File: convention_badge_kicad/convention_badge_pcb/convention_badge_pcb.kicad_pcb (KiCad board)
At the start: 2 copper layers, 11 parts, among them J1 E_Paper_Display, J2 3.7V Battery, SW1 SW_Push, SW2 SW_Push, SW3 SW_Push, SW4 SW_SPST, U1 XIAO-ESP32-C3-DIP

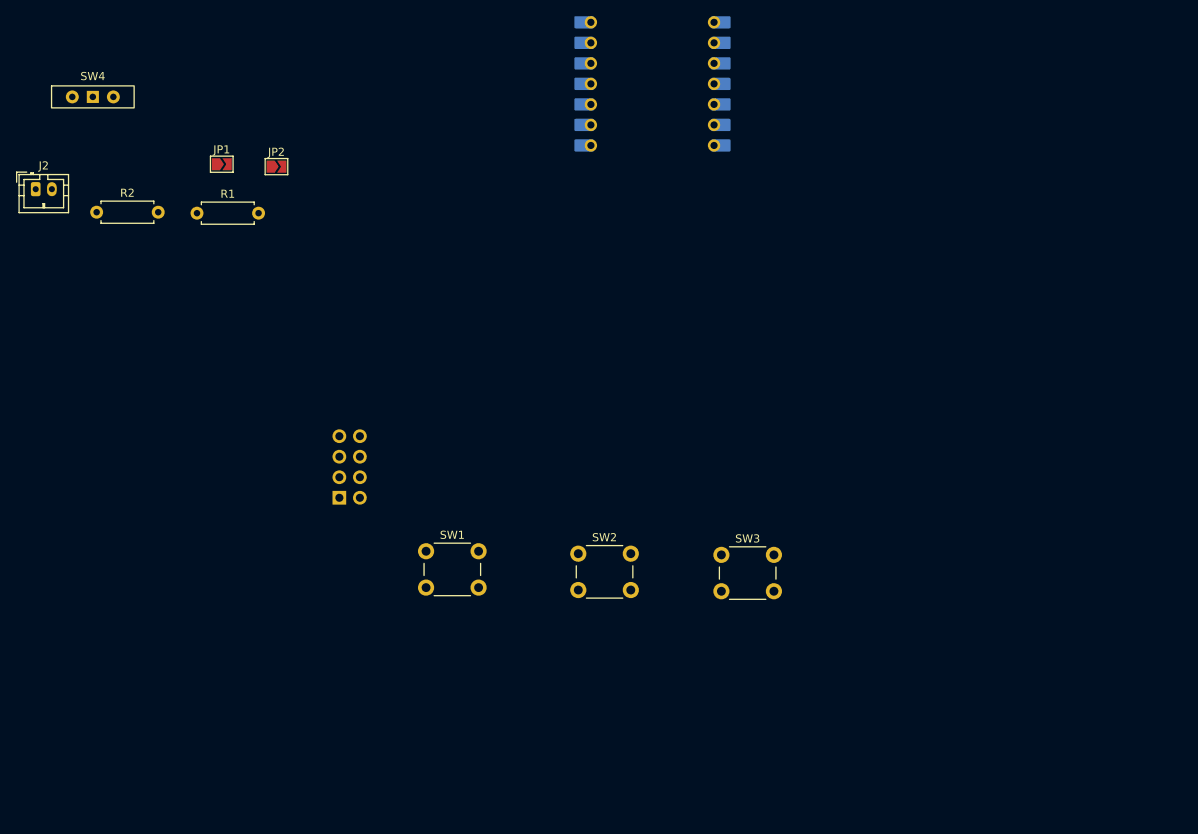
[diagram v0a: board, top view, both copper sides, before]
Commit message: created footprint for display and made a (very) rough layout of the board
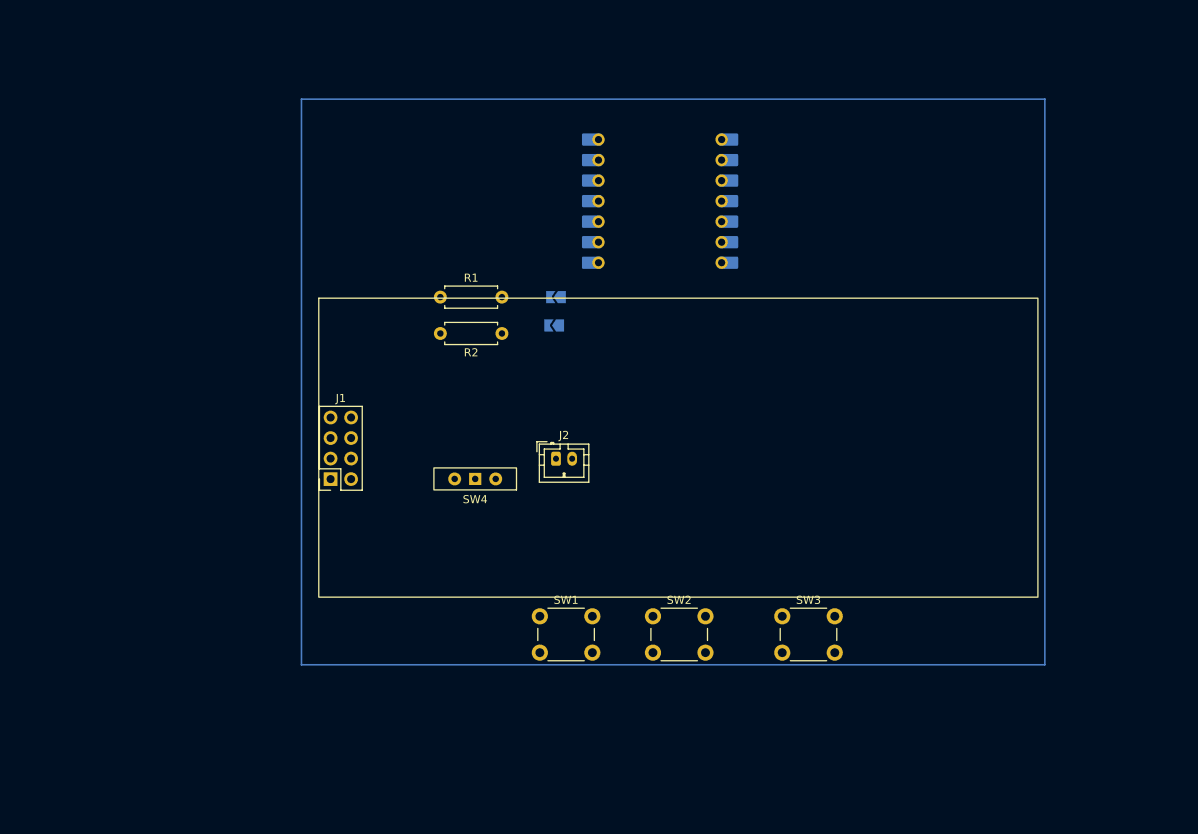
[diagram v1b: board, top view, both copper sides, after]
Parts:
- J1: footprint Connector_PinHeader_2.54mm:PinHeader_2x04_P2.54mm_Vertical -> 2_Displays:2.9_e_paper_ER-EPD029-2-5073; moved to F.Cu
- JP1, JP2: moved to B.Cu
- moved J2 72.5 mm to (127.5, 92.5)
- moved SW4 66.9 mm to (117.5, 95.0), turned to 180 degrees
- moved R2 52.4 mm to (120.8, 77.0), turned to 180 degrees
- moved JP1 44.5 mm to (127.5, 72.5), turned to 180 degrees
- moved JP2 39.6 mm to (127.3, 76.0), turned to 180 degrees
- moved R1 31.9 mm to (113.2, 72.5)
- moved SW1 16.2 mm to (125.5, 112.0)
- moved U1 14.5 mm to (140.4, 60.6)
- moved SW2 12.1 mm to (139.5, 112.0)
- moved J1 11.7 mm to (98.1, 85.9)
- moved SW3 10.7 mm to (155.5, 112.0)

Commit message: finished v1 layout, will serve as backup for if v2 is unfeasable
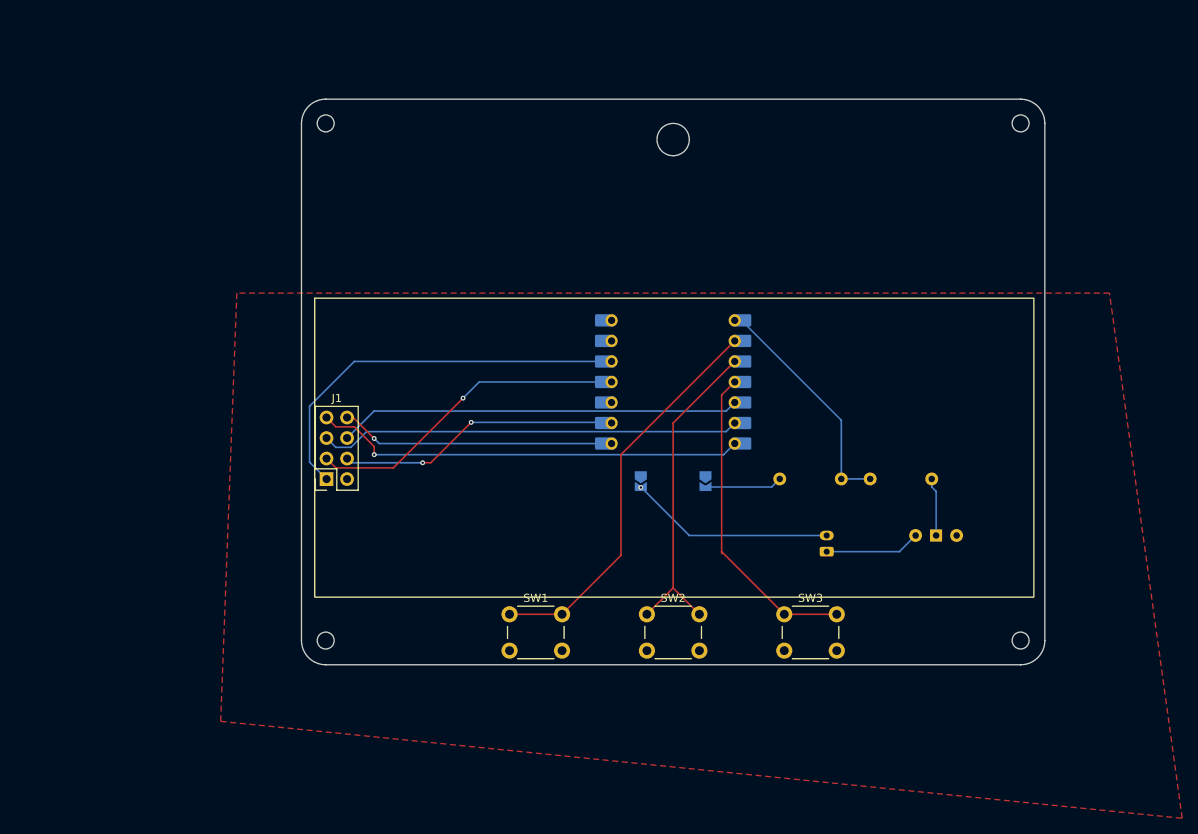
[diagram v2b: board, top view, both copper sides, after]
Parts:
- added ?: , , F.Cu at (142.0, 53.0)
- added ?: , , F.Cu at (117.5, 52.0)
- added REF**: MountingHole_2.1mm, MountingHole:MountingHole_2.1mm, F.Cu at (185.0, 115.0)
- added REF**: MountingHole_2.1mm, MountingHole:MountingHole_2.1mm, F.Cu at (185.0, 51.0)
- added REF**: MountingHole_2.1mm, MountingHole:MountingHole_2.1mm, F.Cu at (99.0, 51.0)
- added REF**: MountingHole_2.1mm, MountingHole:MountingHole_2.1mm, F.Cu at (117.5, 52.0)
- added REF**: MountingHole_2.1mm, MountingHole:MountingHole_2.1mm, F.Cu at (166.5, 52.0)
- added REF**: MountingHole_2.1mm, MountingHole:MountingHole_2.1mm, F.Cu at (99.0, 115.0)
- J2: footprint Connector_JST:JST_PH_B2B-PH-K_1x02_P2.00mm_Vertical -> Connector_JST:JST_PH_S2B-PH-K_1x02_P2.00mm_Horizontal; moved to B.Cu
- R1, R2, SW4: moved to B.Cu
- moved SW4 57.5 mm to (174.5, 102.0), turned to 0 degrees
- moved R2 56.2 mm to (174.0, 95.0)
- moved R1 54.5 mm to (162.8, 95.0), turned to 180 degrees
- moved J2 35.4 mm to (161.0, 104.0), turned to 90 degrees
- moved JP1 29.3 mm to (146.0, 95.3), turned to -90 degrees
- moved U1 22.4 mm to (142.0, 83.0)
- moved JP2 22.1 mm to (138.0, 95.3), turned to -90 degrees
- moved SW1 3.76 mm to (121.8, 111.8)
- moved SW2 0.79 mm to (138.8, 111.8)
- moved J1 0.50 mm to (97.6, 85.9)
- moved SW3 0.35 mm to (155.8, 111.8)
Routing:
- net /RET: track 0.00 -> 54.4 mm, vias 0 -> 1
- net /CS: track 0.00 -> 52.2 mm
- net /DC: track 0.00 -> 49.8 mm
- net /BUT_1: track 0.00 -> 49.2 mm
- net /VDD: track 0.00 -> 48.7 mm
- net /BUT_2: track 0.00 -> 40.4 mm
- net /BUT_3: track 0.00 -> 39.4 mm
- net /SDA: track 0.00 -> 39.3 mm, vias 0 -> 1
- net /SCL: track 0.00 -> 34.2 mm, vias 0 -> 2
- net /BUSY: track 0.00 -> 33.2 mm, vias 0 -> 1
- net /ADC: track 0.00 -> 28.3 mm
- net GND: track 0.00 -> 25.0 mm, vias 0 -> 1
- net +3.7V: track 0.00 -> 12.4 mm
- net Net-(JP1-B): track 0.00 -> 9.60 mm
- net Net-(SW4-A): track 0.00 -> 7.22 mm
- added copper zone on F.Cu, net GND
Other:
- board outline added: 92 x 70 mm

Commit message: modified the board and generated gerbers
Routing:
- net /ADC: track 28.3 -> 31.6 mm
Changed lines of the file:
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@@
 		(tenting front back)
 		(pcbplotparams
-			(layerselection 0x00000000_00000000_55555555_5755f5ff)
+			(layerselection 0x00000000_00000000_55555555_575555ff)
 			(plot_on_all_layers_selection 0x00000000_00000000_00000000_00000000)
 			(disableapertmacros no)
@@
 			(usegerberattributes yes)
 			(usegerberadvancedattributes yes)
-			(creategerberjobfile yes)
+			(creategerberjobfile no)
 			(dashed_line_dash_ratio 12.000000)
 			(dashed_line_gap_ratio 3.000000)
@@
 			(outputformat 1)
 			(mirror no)
-			(drillshape 1)
+			(drillshape 0)
 			(scaleselection 1)
-			(outputdirectory "")
+			(outputdirectory "Gerbers/")
 		)
 	)
@@
 		(layer "Edge.Cuts")
 	)
+	(dimension
+		(type orthogonal)
+		(layer "User.1")
+		(pts
+			(xy 188 115) (xy 96 115)
+		)
+		(height 12)
+		(orientation 0)
+		(format
+			(prefix "")
+			(suffix "")
+			(units 3)
+			(units_format 0)
+			(precision 4)
+			(suppress_zeroes yes)
+		)
+		(style
+			(thickness 0.1)
+			(arrow_length 1.27)
+			(text_position_mode 0)
+			(arrow_direction outward)
+			(extension_height 0.58642)
+			(extension_offset 0.5)
+			(keep_text_aligned yes)
+		)
+		(gr_text "92"
+			(at 142 125.85 0)
+			(layer "User.1")
+			(effects
+				(font
+					(size 1 1)
+					(thickness 0.15)
+				)
+			)
+		)
+	)
+	(dimension
+		(type orthogonal)
+		(layer "User.1")
+		(pts
+			(xy 185 48) (xy 185 118)
+		)
+		(height 11)
+		(orientation 1)
+		(format
+			(prefix "")
+			(suffix "")
+			(units 3)
+			(units_format 0)
+			(precision 4)
+			(suppress_zeroes yes)
+		)
+		(style
+			(thickness 0.1)
+			(arrow_length 1.27)
+			(text_position_mode 0)
+			(arrow_direction outward)
+			(extension_height 0.58642)
+			(extension_offset 0.5)
+			(keep_text_aligned yes)
+		)
+		(gr_text "70"
+			(at 194.85 83 90)
+			(layer "User.1")
+			(effects
+				(font
+					(size 1 1)
+					(thickness 0.15)
+				)
+			)
+		)
+	)
 	(segment
 		(start 133.545 80.46)
@@
 	)
 	(segment
-		(start 107.369 93.631)
-		(end 100.2535 93.631)
+		(start 100.4125 93.79)
+		(end 99.1025 92.48)
 		(width 0.2)
 		(layer "F.Cu")
@@
 	)
 	(segment
-		(start 100.2535 93.631)
-		(end 99.1025 92.48)
+		(start 116 85)
+		(end 107.21 93.79)
 		(width 0.2)
 		(layer "F.Cu")
@@
 	)
 	(segment
-		(start 116 85)
-		(end 107.369 93.631)
+		(start 107.21 93.79)
+		(end 100.4125 93.79)
 		(width 0.2)
 		(layer "F.Cu")
@@
 	)
 	(segment
-		(start 148.557 89.143)
-		(end 104.06726 89.143)
+		(start 148.36 89.34)
+		(end 104.1 89.34)
 		(width 0.2)
 		(layer "B.Cu")
@@
 	)
 	(segment
-		(start 102.11926 91.091)
-		(end 100.2535 91.091)
+		(start 149.62 88.08)
+		(end 148.36 89.34)
 		(width 0.2)
 		(layer "B.Cu")
@@
 	)
 	(segment
-		(start 149.62 88.08)
-		(end 148.557 89.143)
+		(start 102.18 91.26)
+		(end 100.4225 91.26)
 		(width 0.2)
 		(layer "B.Cu")
@@
 	)
 	(segment
-		(start 100.2535 91.091)
+		(start 100.4225 91.26)
 		(end 99.1025 89.94)
 		(width 0.2)
@@
 	)
 	(segment
-		(start 104.06726 89.143)
-		(end 102.11926 91.091)
+		(start 104.1 89.34)
+		(end 102.18 91.26)
 		(width 0.2)
 		(layer "B.Cu")
@@
 	)
 	(segment
-		(start 102.551 88.551)
-		(end 100.2535 88.551)
+		(start 105 91)
+		(end 102.65 88.65)
 		(width 0.2)
 		(layer "F.Cu")
@@
 	)
 	(segment
-		(start 100.2535 88.551)
-		(end 99.1025 87.4)
+		(start 105 92)
+		(end 105 91)
 		(width 0.2)
 		(layer "F.Cu")
@@
 	)
 	(segment
-		(start 105 92)
-		(end 105 91)
+		(start 100.3525 88.65)
+		(end 99.1025 87.4)
 		(width 0.2)
 		(layer "F.Cu")
@@
 	)
 	(segment
-		(start 105 91)
-		(end 102.551 88.551)
+		(start 102.65 88.65)
+		(end 100.3525 88.65)
 		(width 0.2)
 		(layer "F.Cu")
@@
 	)
 	(segment
-		(start 104.9795 86.603)
-		(end 101.6425 89.94)
+		(start 149.62 85.54)
+		(end 148.32 86.84)
 		(width 0.2)
 		(layer "B.Cu")
@@
 	)
 	(segment
-		(start 148.557 86.603)
-		(end 104.9795 86.603)
+		(start 148.32 86.84)
+		(end 104.7425 86.84)
 		(width 0.2)
 		(layer "B.Cu")
@@
 	)
 	(segment
-		(start 149.62 85.54)
-		(end 148.557 86.603)
+		(start 104.7425 86.84)
+		(end 101.6425 89.94)
 		(width 0.2)
 		(layer "B.Cu")
@@
 	)
 	(segment
-		(start 162.81 95)
-		(end 162.81 87.735)
+		(start 162.81 82.14)
+		(end 156.05 75.38)
 		(width 0.2)
 		(layer "B.Cu")
@@
 	)
 	(segment
-		(start 162.81 87.735)
+		(start 156.05 75.38)
 		(end 150.455 75.38)
 		(width 0.2)
@@
 	)
 	(segment
-		(start 135.54 92)
-		(end 135.54 104.46)
+		(start 162.81 95)
+		(end 162.81 82.14)
+		(width 0.2)
+		(layer "B.Cu")
+		(net 11)
+	)
+	(segment
+		(start 149.62 77.92)
+		(end 136 91.54)
 		(width 0.2)
 		(layer "F.Cu")
@@
 	)
 	(segment
-		(start 135.54 104.46)
+		(start 136 104)
 		(end 128.25 111.75)
 		(width 0.2)
@@
 	)
 	(segment
-		(start 149.62 77.92)
-		(end 135.54 92)
+		(start 136 91.54)
+		(end 136 104)
 		(width 0.2)
 		(layer "F.Cu")
